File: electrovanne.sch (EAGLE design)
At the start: 14 parts, among them IC1 7805TV, T1 2N2222, T2 2N2222, X1 MKDSN1,5/2-5,08

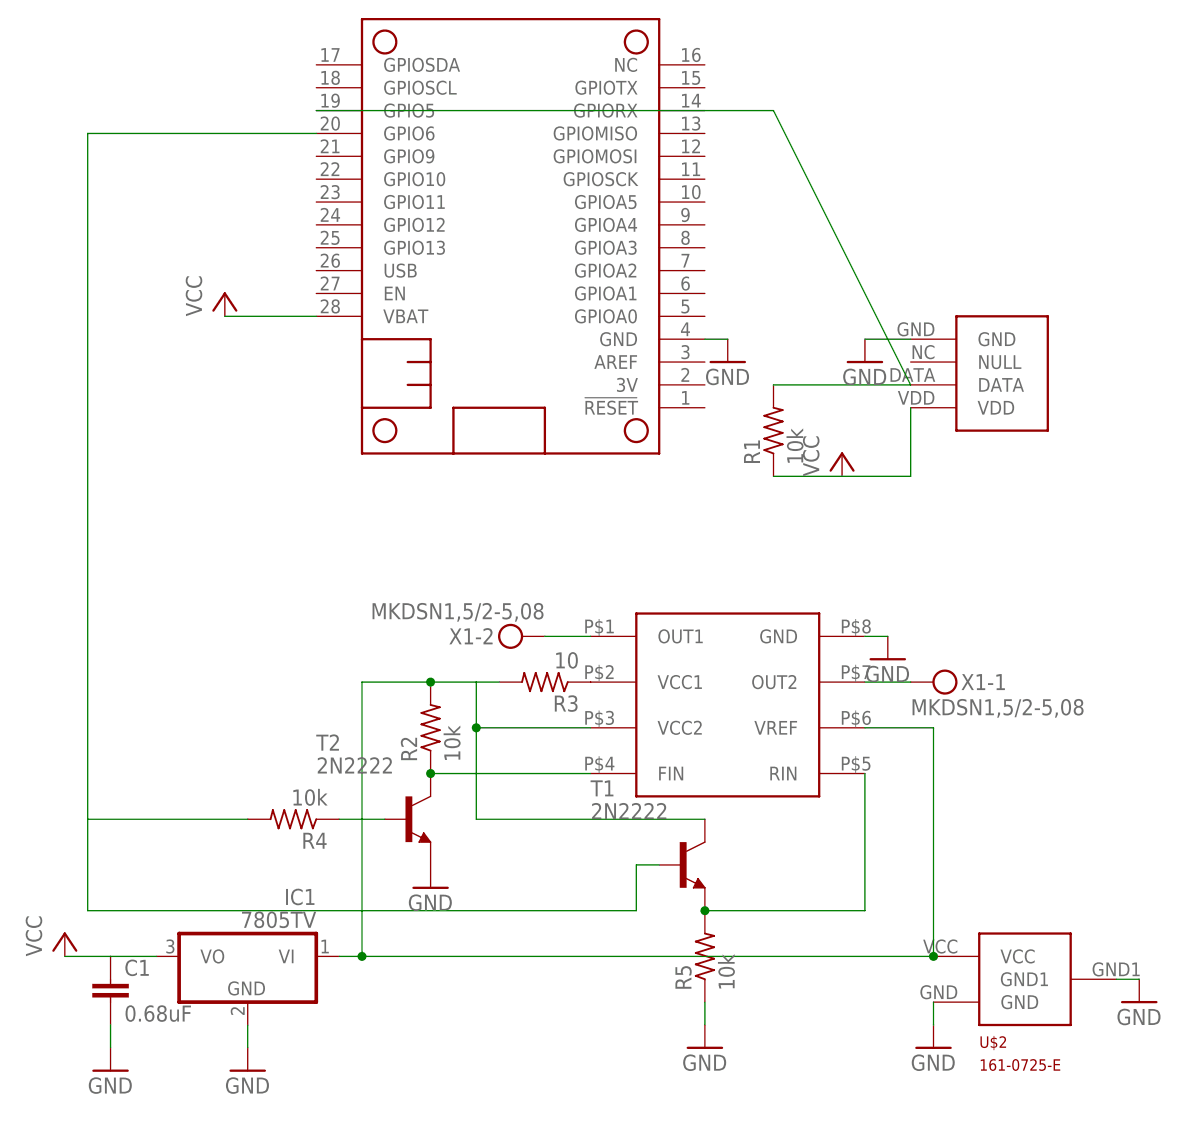
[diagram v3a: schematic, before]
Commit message: version 3: pb wit the RIN inverter
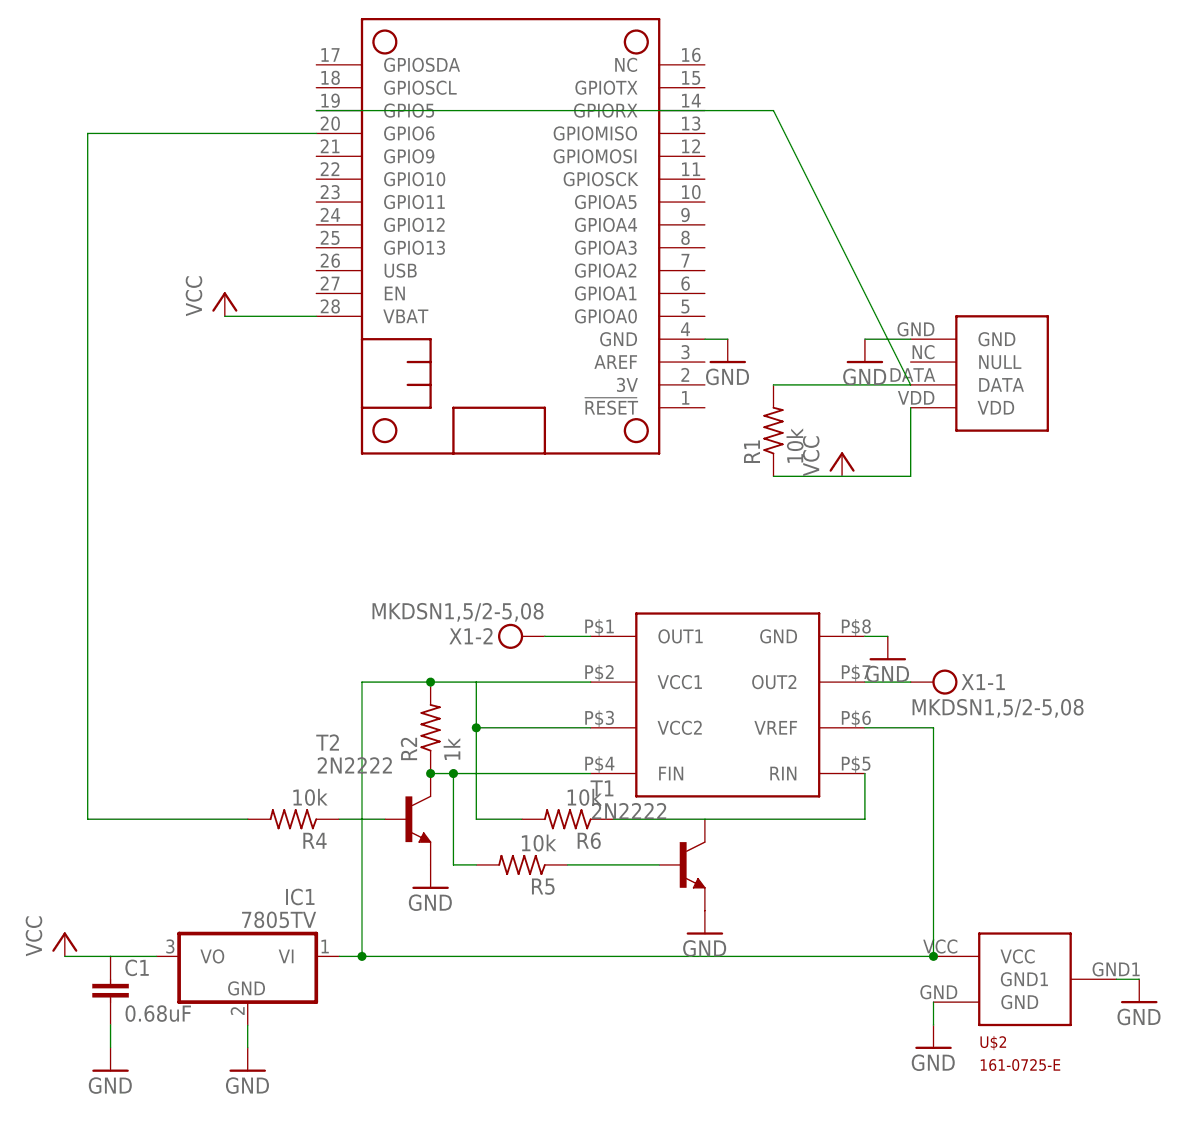
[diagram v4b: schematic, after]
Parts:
- removed R3: 10, resistor:R-US_R0603
- added R6: 10k, resistor:R-US_R0603
- R2: value 10k -> 1k
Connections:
- removed net N$5: R3.1, U$4.VCC1
- new net N$10: R6.1, T1.C, U$4.RIN
- net GND: now also T1.E; no longer R5.1
- net N$1: now also R6.2, U$4.VCC1; no longer R3.2, T1.C
- net N$2: now also R5.1, T1.B; no longer R5.2, T1.E, U$4.RIN
- net N$7: no longer T1.B
- net N$8: now also R5.2
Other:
- moved on the sheet: R5
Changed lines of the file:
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@@
 <part name="T2" library="transistor" deviceset="2N2222" device=""/>
 <part name="GND5" library="supply1" deviceset="GND" device=""/>
-<part name="R5" library="resistor" deviceset="R-US_" device="R0603" value="10k"/>
-<part name="R2" library="resistor" deviceset="R-US_" device="R0603" value="10k"/>
+<part name="R2" library="resistor" deviceset="R-US_" device="R0603" value="1k"/>
 <part name="R1" library="resistor" deviceset="R-US_" device="R0603" value="10k"/>
 <part name="IC1" library="linear" deviceset="78*" device="TV" technology="05"/>
@@
 <part name="GND10" library="supply1" deviceset="GND" device=""/>
 <part name="R4" library="resistor" deviceset="R-US_" device="R0603" value="10k"/>
-<part name="R3" library="resistor" deviceset="R-US_" device="R0603" value="10"/>
+<part name="R6" library="resistor" deviceset="R-US_" device="R0603" value="10k"/>
+<part name="R5" library="resistor" deviceset="R-US_" device="R0603" value="10k"/>
 </parts>
 <sheets>
@@
 <instance part="T2" gate="G$1" x="20.32" y="2.54"/>
 <instance part="GND5" gate="1" x="22.86" y="-5.08"/>
-<instance part="R5" gate="G$1" x="53.34" y="-12.7" rot="R90"/>
 <instance part="R2" gate="G$1" x="22.86" y="12.7" rot="R90"/>
 <instance part="R1" gate="G$1" x="60.96" y="45.72" rot="R90"/>
 <instance part="IC1" gate="A1" x="2.54" y="-12.7" rot="MR0"/>
-<instance part="GND6" gate="1" x="53.34" y="-22.86"/>
+<instance part="GND6" gate="1" x="53.34" y="-10.16"/>
 <instance part="GND7" gate="1" x="78.74" y="-22.86"/>
 <instance part="GND8" gate="1" x="101.6" y="-17.78"/>
@@
 <instance part="GND10" gate="1" x="-12.7" y="-25.4"/>
 <instance part="R4" gate="G$1" x="7.62" y="2.54" rot="R180"/>
-<instance part="R3" gate="G$1" x="35.56" y="17.78" rot="R180"/>
+<instance part="R6" gate="G$1" x="38.1" y="2.54" rot="R180"/>
+<instance part="R5" gate="G$1" x="33.02" y="-2.54" rot="R180"/>
 </instances>
 <busses>
@@
 </segment>
 <segment>
-<pinref part="R5" gate="G$1" pin="1"/>
-<pinref part="GND6" gate="1" pin="GND"/>
-<wire x1="53.34" y1="-20.32" x2="53.34" y2="-17.78" width="0.1524" layer="91"/>
-</segment>
-<segment>
 <pinref part="U$2" gate="G$1" pin="GND"/>
 <pinref part="GND7" gate="1" pin="GND"/>
@@
 <pinref part="T2" gate="G$1" pin="E"/>
 <pinref part="GND5" gate="1" pin="GND"/>
+</segment>
+<segment>
+<pinref part="T1" gate="G$1" pin="E"/>
+<pinref part="GND6" gate="1" pin="GND"/>
 </segment>
 </net>
@@
 <wire x1="15.24" y1="17.78" x2="22.86" y2="17.78" width="0.1524" layer="91"/>
 <wire x1="22.86" y1="17.78" x2="27.94" y2="17.78" width="0.1524" layer="91"/>
-<pinref part="T1" gate="G$1" pin="C"/>
 <wire x1="27.94" y1="17.78" x2="27.94" y2="12.7" width="0.1524" layer="91"/>
 <wire x1="27.94" y1="12.7" x2="27.94" y2="2.54" width="0.1524" layer="91"/>
-<wire x1="27.94" y1="2.54" x2="53.34" y2="2.54" width="0.1524" layer="91"/>
 <pinref part="R2" gate="G$1" pin="2"/>
 <junction x="22.86" y="17.78"/>
@@
 <pinref part="U$4" gate="G$1" pin="VCC2"/>
 <wire x1="40.64" y1="12.7" x2="27.94" y2="12.7" width="0.1524" layer="91"/>
-<pinref part="R3" gate="G$1" pin="2"/>
-<wire x1="30.48" y1="17.78" x2="27.94" y2="17.78" width="0.1524" layer="91"/>
 <junction x="15.24" y="-12.7"/>
 <junction x="27.94" y="12.7"/>
+<pinref part="R6" gate="G$1" pin="2"/>
+<wire x1="27.94" y1="2.54" x2="33.02" y2="2.54" width="0.1524" layer="91"/>
+<pinref part="U$4" gate="G$1" pin="VCC1"/>
+<wire x1="27.94" y1="17.78" x2="40.64" y2="17.78" width="0.1524" layer="91"/>
 </segment>
 </net>
@@
 </segment>
 </net>
-<net name="N$2" class="0">
-<segment>
-<pinref part="T1" gate="G$1" pin="E"/>
-<pinref part="U$4" gate="G$1" pin="RIN"/>
-<wire x1="53.34" y1="-7.62" x2="71.12" y2="-7.62" width="0.1524" layer="91"/>
-<wire x1="71.12" y1="-7.62" x2="71.12" y2="7.62" width="0.1524" layer="91"/>
-<pinref part="R5" gate="G$1" pin="2"/>
-<junction x="53.34" y="-7.62"/>
-</segment>
-</net>
 <net name="N$8" class="0">
 <segment>
 <pinref part="T2" gate="G$1" pin="C"/>
 <pinref part="U$4" gate="G$1" pin="FIN"/>
-<wire x1="22.86" y1="7.62" x2="40.64" y2="7.62" width="0.1524" layer="91"/>
+<wire x1="22.86" y1="7.62" x2="25.4" y2="7.62" width="0.1524" layer="91"/>
 <pinref part="R2" gate="G$1" pin="1"/>
 <junction x="22.86" y="7.62"/>
+<wire x1="25.4" y1="7.62" x2="40.64" y2="7.62" width="0.1524" layer="91"/>
+<wire x1="25.4" y1="7.62" x2="25.4" y2="-2.54" width="0.1524" layer="91"/>
+<junction x="25.4" y="7.62"/>
+<pinref part="R5" gate="G$1" pin="2"/>
+<wire x1="27.94" y1="-2.54" x2="25.4" y2="-2.54" width="0.1524" layer="91"/>
 </segment>
 </net>
 <net name="N$7" class="0">
 <segment>
-<pinref part="T1" gate="G$1" pin="B"/>
-<wire x1="45.72" y1="-2.54" x2="48.26" y2="-2.54" width="0.1524" layer="91"/>
-<wire x1="45.72" y1="-7.62" x2="45.72" y2="-2.54" width="0.1524" layer="91"/>
 <pinref part="MS1" gate="G$1" pin="GPIO6"/>
 <wire x1="10.16" y1="78.74" x2="-15.24" y2="78.74" width="0.1524" layer="91"/>
 <wire x1="-15.24" y1="78.74" x2="-15.24" y2="2.54" width="0.1524" layer="91"/>
-<wire x1="-15.24" y1="2.54" x2="-15.24" y2="-7.62" width="0.1524" layer="91"/>
-<wire x1="45.72" y1="-7.62" x2="-15.24" y2="-7.62" width="0.1524" layer="91"/>
 <wire x1="-15.24" y1="2.54" x2="2.54" y2="2.54" width="0.1524" layer="91"/>
 <pinref part="R4" gate="G$1" pin="2"/>
@@
 </segment>
 </net>
-<net name="N$5" class="0">
-<segment>
-<pinref part="U$4" gate="G$1" pin="VCC1"/>
-<pinref part="R3" gate="G$1" pin="1"/>
-</segment>
-</net>
+<net name="N$10" class="0">
+<segment>
+<pinref part="R6" gate="G$1" pin="1"/>
+<pinref part="T1" gate="G$1" pin="C"/>
+<wire x1="43.18" y1="2.54" x2="53.34" y2="2.54" width="0.1524" layer="91"/>
+<pinref part="U$4" gate="G$1" pin="RIN"/>
+<wire x1="71.12" y1="2.54" x2="71.12" y2="7.62" width="0.1524" layer="91"/>
+<wire x1="53.34" y1="2.54" x2="71.12" y2="2.54" width="0.1524" layer="91"/>
+</segment>
+</net>
+<net name="N$2" class="0">
+<segment>
+<pinref part="T1" gate="G$1" pin="B"/>
+<pinref part="R5" gate="G$1" pin="1"/>
+<wire x1="48.26" y1="-2.54" x2="38.1" y2="-2.54" width="0.1524" layer="91"/>
+</segment>
+</net>
